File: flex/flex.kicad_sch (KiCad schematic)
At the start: 93 parts, among them J1 Conn_01x06_Female, J2 Conn_01x05_Female, J3 Conn_01x03_Female, J4 Conn_01x06_Female, J5 Conn_01x03_Female, SW1 SW_Push, SW10 SW_Push, SW11 SW_Push, SW12 SW_Push, SW14 SW_Push, SW15 SW_Push, SW16 SW_Push, SW17 SW_Push, SW19 SW_Push, SW2 SW_Push, SW20 SW_Push, SW21 SW_Push, SW22 SW_Push, SW23 SW_Push, SW24 SW_Push, SW25 SW_Push, SW26 SW_Push, SW3 SW_Push, SW4 SW_Push, SW5 SW_Push, SW6 SW_Push, SW7 SW_Push, SW8 SW_Push, SW9 SW_Push

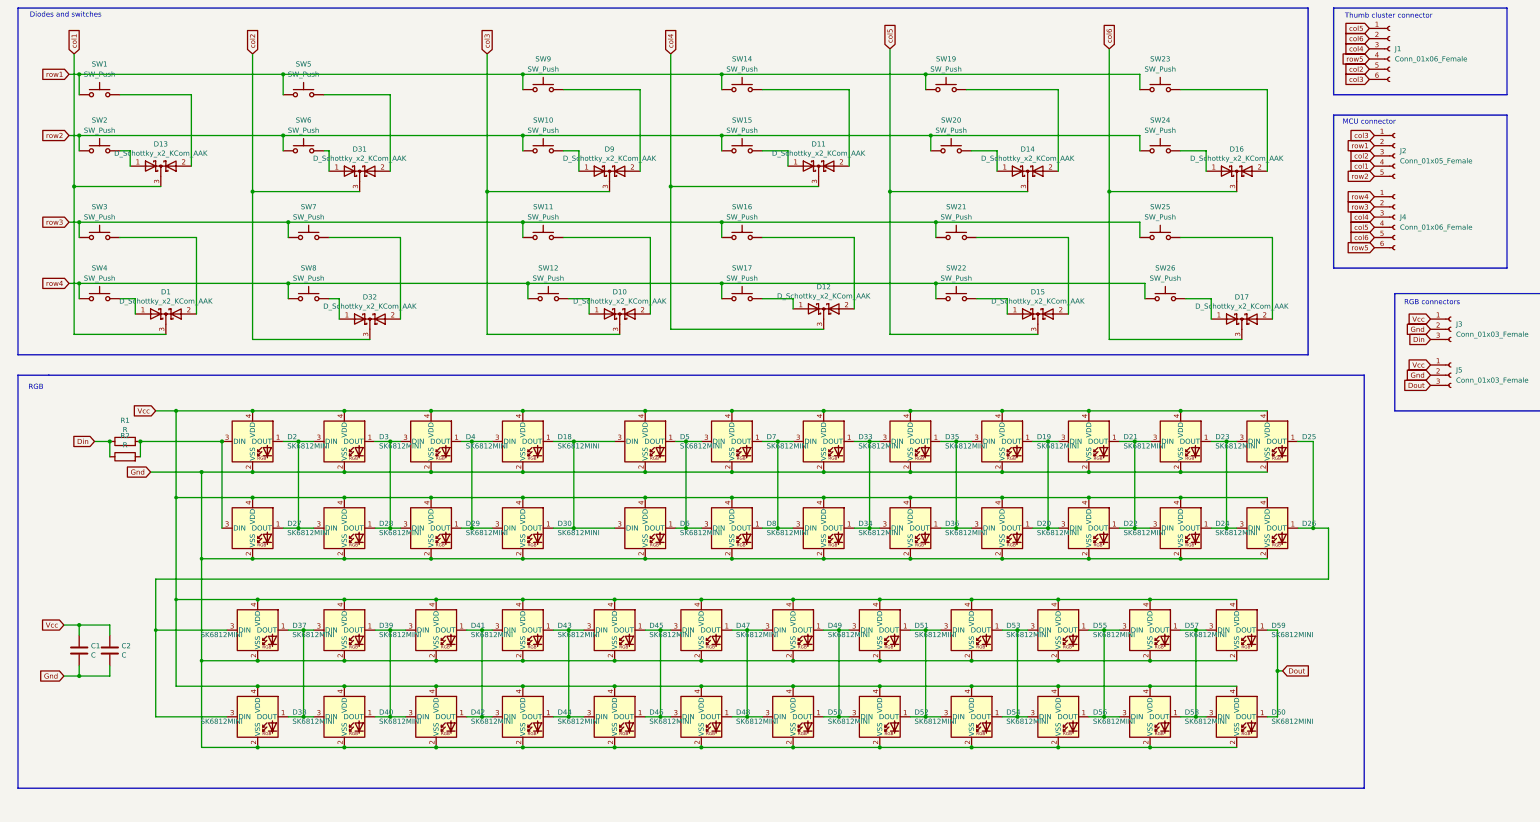
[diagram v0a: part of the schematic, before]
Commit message: update diodes and leds
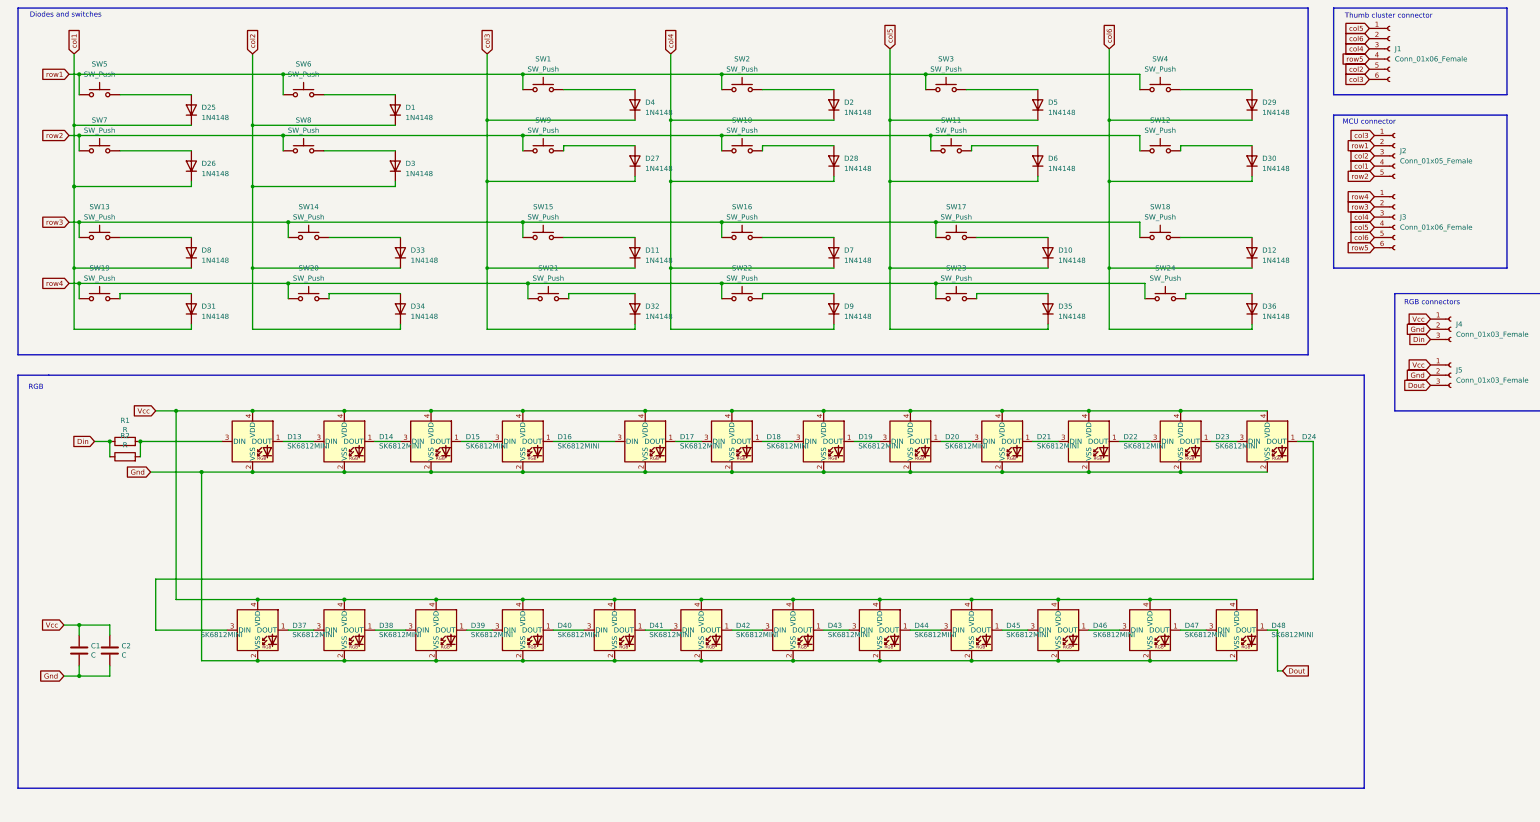
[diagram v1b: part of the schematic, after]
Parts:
- removed D1, D10, D11, D12, D13, D14, D15, D16, D17, D31, D32, D9: D_Schottky_x2_KCom_AAK, customs:TSOT-23_HandSoldering, symbol Device:D_Schottky_x2_KCom_AAK
- removed D20, D22, D24, D26, D27, D28, D29, D30, D34, D36, D38, D40, D42, D44, D46, D48, D50, D52, D54, D56, D58, D6, D60, D8: SK6812MINI, libs2:YS-SK6812MINI-E_REVERSE_NO_EDGECUT, symbol LED:SK6812MINI
- added D1, D10, D11, D12, D2, D25, D26, D27, D28, D29, D3, D30, D31, D32, D33, D34, D35, D36, D4, D5, D6, D7, D8, D9: 1N4148, libs:D_0402, symbol Diode:1N4148
- D13: renamed from D2; footprint libs2:YS-SK6812MINI-E_REVERSE -> libs:SK6812_mini_e_corners
- D14: renamed from D3; footprint libs2:YS-SK6812MINI-E_REVERSE -> libs:SK6812_mini_e_corners
- D15: renamed from D4; footprint libs2:YS-SK6812MINI-E_REVERSE -> libs:SK6812_mini_e_corners
- D16: renamed from D18; footprint libs2:YS-SK6812MINI-E_REVERSE -> libs:SK6812_mini_e_corners
- D17: renamed from D5; footprint libs2:YS-SK6812MINI-E_REVERSE -> libs:SK6812_mini_e_corners
- D18: renamed from D7; footprint libs2:YS-SK6812MINI-E_REVERSE -> libs:SK6812_mini_e_corners
- D19: renamed from D33; footprint libs2:YS-SK6812MINI-E_REVERSE -> libs:SK6812_mini_e_corners
- D20: renamed from D35; footprint libs2:YS-SK6812MINI-E_REVERSE -> libs:SK6812_mini_e_corners
- D21: renamed from D19; footprint libs2:YS-SK6812MINI-E_REVERSE -> libs:SK6812_mini_e_corners
- D22: renamed from D21; footprint libs2:YS-SK6812MINI-E_REVERSE -> libs:SK6812_mini_e_corners
- D23, D37: footprint libs2:YS-SK6812MINI-E_REVERSE -> libs:SK6812_mini_e_corners
- D24: renamed from D25; footprint libs2:YS-SK6812MINI-E_REVERSE -> libs:SK6812_mini_e_corners
- D38: renamed from D39; footprint libs2:YS-SK6812MINI-E_REVERSE -> libs:SK6812_mini_e_corners
- D39: renamed from D41; footprint libs2:YS-SK6812MINI-E_REVERSE -> libs:SK6812_mini_e_corners
- D40: renamed from D43; footprint libs2:YS-SK6812MINI-E_REVERSE -> libs:SK6812_mini_e_corners
- D41: renamed from D45; footprint libs2:YS-SK6812MINI-E_REVERSE -> libs:SK6812_mini_e_corners
- D42: renamed from D47; footprint libs2:YS-SK6812MINI-E_REVERSE -> libs:SK6812_mini_e_corners
- D43: renamed from D49; footprint libs2:YS-SK6812MINI-E_REVERSE -> libs:SK6812_mini_e_corners
- D44: renamed from D51; footprint libs2:YS-SK6812MINI-E_REVERSE -> libs:SK6812_mini_e_corners
- D45: renamed from D53; footprint libs2:YS-SK6812MINI-E_REVERSE -> libs:SK6812_mini_e_corners
- D46: renamed from D55; footprint libs2:YS-SK6812MINI-E_REVERSE -> libs:SK6812_mini_e_corners
- D47: renamed from D57; footprint libs2:YS-SK6812MINI-E_REVERSE -> libs:SK6812_mini_e_corners
- D48: renamed from D59; footprint libs2:YS-SK6812MINI-E_REVERSE -> libs:SK6812_mini_e_corners
- renumbered J4 to J3, J3 to J4, SW9 to SW1, SW15 to SW10, SW20 to SW11, SW24 to SW12, SW3 to SW13, SW7 to SW14, SW11 to SW15, SW21 to SW17, SW25 to SW18, SW4 to SW19, SW14 to SW2, SW8 to SW20, SW12 to SW21, SW17 to SW22, SW22 to SW23, SW26 to SW24, SW19 to SW3, SW23 to SW4, SW1 to SW5, SW5 to SW6, SW2 to SW7, SW6 to SW8, SW10 to SW9
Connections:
- net col1: now also D25.1 (K), D26.1 (K), D31.1 (K), D8.1 (K)
- net col2: now also D1.1 (K), D3.1 (K), D33.1 (K), D34.1 (K)
- net col3: now also D11.1 (K), D27.1 (K), D32.1 (K), D4.1 (K)
- net col4: now also D2.1 (K), D28.1 (K), D7.1 (K), D9.1 (K)
- net col5: now also D10.1 (K), D35.1 (K), D5.1 (K), D6.1 (K)
- net col6: now also D12.1 (K), D29.1 (K), D30.1 (K), D36.1 (K)
- net at SW23.2: now also D35.2 (A)
- net at SW17.2: now also D10.2 (A)
- net at SW7.2: now also D26.2 (A)
- net at SW24.2: now also D36.2 (A)
- net at SW18.2: now also D12.2 (A)
- net at SW6.2: now also D1.2 (A)
- net at SW15.2: now also D11.2 (A)
- net at SW21.2: now also D32.2 (A)
- net at SW20.2: now also D34.2 (A)
- net at SW22.2: now also D9.2 (A)
- net at SW16.2: now also D7.2 (A)
- net at SW8.2: now also D3.2 (A)
- net at SW5.2: now also D25.2 (A)
- net at SW13.2: now also D8.2 (A)
- net at SW2.2: now also D2.2 (A)
- net at SW12.2: now also D30.2 (A)
- net at SW9.2: now also D27.2 (A)
- net at SW1.2: now also D4.2 (A)
- net at SW11.2: now also D6.2 (A)
- net at SW10.2: now also D28.2 (A)
- net at SW19.2: now also D31.2 (A)
- net at SW3.2: now also D5.2 (A)
- net at SW14.2: now also D33.2 (A)
- net at SW4.2: now also D29.2 (A)

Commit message: emergency diodes
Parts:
- added D49, D50, D51, D52, D53, D54, D55, D56, D57, D58, D59, D60, D61, D62, D63, D64, D65, D66, D67, D68, D69, D70, D71, D72: 1N4148, custom:Diode_TH_SOD123, symbol Diode:1N4148
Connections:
- net col1: now also D49.1 (K), D50.1 (K), D51.1 (K), D52.1 (K)
- net col2: now also D53.1 (K), D54.1 (K), D55.1 (K), D56.1 (K)
- net col3: now also D57.1 (K), D58.1 (K), D59.1 (K), D60.1 (K)
- net col4: now also D61.1 (K), D62.1 (K), D63.1 (K), D64.1 (K)
- net col5: now also D65.1 (K), D66.1 (K), D67.1 (K), D68.1 (K)
- net col6: now also D69.1 (K), D70.1 (K), D71.1 (K)
- net at D26.2 (A), SW7.2: now also D50.2 (A)
- net at D25.2 (A), SW5.2: now also D49.2 (A)
- net at D35.2 (A), SW23.2: now also D68.2 (A)
- net at D28.2 (A), SW10.2: now also D62.2 (A)
- net at D7.2 (A), SW16.2: now also D63.2 (A)
- net at D30.2 (A), SW12.2: now also D70.2 (A)
- net at D11.2 (A), SW15.2: now also D59.2 (A)
- net at D27.2 (A), SW9.2: now also D58.2 (A)
- net at D1.2 (A), SW6.2: now also D53.2 (A)
- net at D32.2 (A), SW21.2: now also D60.2 (A)
- net at D34.2 (A), SW20.2: now also D56.2 (A)
- net at D3.2 (A), SW8.2: now also D54.2 (A)
- net at D8.2 (A), SW13.2: now also D51.2 (A)
- net at D6.2 (A), SW11.2: now also D66.2 (A)
- net at D2.2 (A), SW2.2: now also D61.2 (A)
- net at D31.2 (A), SW19.2: now also D52.2 (A)
- net at D9.2 (A), SW22.2: now also D64.2 (A)
- net at D12.2 (A), SW18.2: now also D71.2 (A)
- net at D10.2 (A), SW17.2: now also D67.2 (A)
- net at D4.2 (A), SW1.2: now also D57.2 (A)
- net at D33.2 (A), SW14.2: now also D55.2 (A)
- net at D5.2 (A), SW3.2: now also D65.2 (A)
- net at D29.2 (A), SW4.2: now also D69.2 (A)
- net at D36.2 (A), SW24.2: now also D72.2 (A)

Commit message: routing
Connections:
- net col6: now also D72.1 (K)
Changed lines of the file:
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@@
   (junction (at 125.73 119.38) (diameter 1.016) (color 0 0 0 0)
   )
+  (junction (at 317.5 99.06) (diameter 0) (color 0 0 0 0)
+  )
   (junction (at 213.36 76.2) (diameter 0) (color 0 0 0 0)
   )
@@
     (stroke (width 0) (type default))
   )
-  (wire (pts (xy 294.64 99.06) (xy 330.2 99.06))
+  (wire (pts (xy 294.64 99.06) (xy 317.5 99.06))
     (stroke (width 0) (type solid))
   )
@@
     (stroke (width 0) (type solid))
   )
+  (wire (pts (xy 317.5 97.79) (xy 317.5 99.06))
+    (stroke (width 0) (type default))
+  )
   (wire (pts (xy 99.06 40.64) (xy 106.68 40.64))
     (stroke (width 0) (type solid))
@@
     (stroke (width 0) (type solid))
   )
+  (wire (pts (xy 317.5 99.06) (xy 330.2 99.06))
+    (stroke (width 0) (type solid))
+  )

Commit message: routing
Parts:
- removed C2: C, Capacitor_SMD:C_1206_3216Metric_Pad1.42x1.75mm_HandSolder, symbol Device:C
- removed R2: R, Resistor_SMD:R_1206_3216Metric_Pad1.42x1.75mm_HandSolder, symbol Device:R
- added C3: C, custom:C_SOD123, symbol Device:C
- added R3: R, custom:R_SOD123, symbol Device:R
- C1: footprint Capacitor_SMD:C_1206_3216Metric_Pad1.42x1.75mm_HandSolder -> libs:D_0402
- R1: footprint Resistor_SMD:R_1206_3216Metric_Pad1.42x1.75mm_HandSolder -> libs:D_0402
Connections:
- net Din: now also R3.1
- net Gnd: now also C3.2
- net Vcc: now also C3.1
- net at D13.3 (DIN), R1.2: now also R3.2
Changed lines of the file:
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@@
     (stroke (width 0) (type solid))
   )
-  (wire (pts (xy 45.72 127) (xy 45.72 130.81))
-    (stroke (width 0) (type solid))
-  )
   (wire (pts (xy 185.42 46.99) (xy 185.42 62.23))
     (stroke (width 0) (type solid))
@@
     (stroke (width 0) (type default))
   )
+  (wire (pts (xy 45.72 175.26) (xy 52.07 175.26))
+    (stroke (width 0) (type default))
+  )
   (wire (pts (xy 214.63 53.34) (xy 226.06 53.34))
     (stroke (width 0) (type solid))
@@
     (stroke (width 0) (type solid))
   )
+  (wire (pts (xy 45.72 182.88) (xy 52.07 182.88))
+    (stroke (width 0) (type default))
+  )
   (wire (pts (xy 35.56 50.8) (xy 38.1 50.8))
     (stroke (width 0) (type solid))
@@
     (stroke (width 0) (type default))
   )
+  (wire (pts (xy 45.72 127) (xy 45.72 134.62))
+    (stroke (width 0) (type default))
+  )
   (wire (pts (xy 275.59 127) (xy 281.94 127))
     (stroke (width 0) (type solid))
@@
     (stroke (width 0) (type solid))
   )
+  (wire (pts (xy 55.88 134.62) (xy 55.88 144.78))
+    (stroke (width 0) (type solid))
+  )
   (wire (pts (xy 36.83 83.82) (xy 54.61 83.82))
     (stroke (width 0) (type default))
@@
     (stroke (width 0) (type solid))
   )
-  (wire (pts (xy 53.34 127) (xy 53.34 130.81))
+  (wire (pts (xy 53.34 127) (xy 53.34 134.62))
     (stroke (width 0) (type solid))
   )
@@
     )
   )
-  (global_label "Gnd" (shape input) (at 55.88 134.62 180)
+  (global_label "Gnd" (shape input) (at 55.88 144.78 180)
     (effects (font (size 1.27 1.27)) (justify right))
-    (property "Intersheetrefs" "${INTERSHEET_REFS}" (at 25.4 -3.81 0)
+    (property "Intersheetrefs" "${INTERSHEET_REFS}" (at 25.4 6.35 0)
       (effects (font (size 1.27 1.27)) hide)
     )
@@
       (effects (font (size 1.27 1.27)) (justify left))
     )
-    (property "Footprint" "Capacitor_SMD:C_1206_3216Metric_Pad1.42x1.75mm_HandSolder" (at 39.0652 182.88 0)
+    (property "Footprint" "libs:D_0402" (at 39.0652 182.88 0)
       (effects (font (size 1.27 1.27)) hide)
     )
@@
     )
   )
-  (symbol (lib_id "Device:C") (at 45.72 179.07 0) (unit 1)
-    (in_bom yes) (on_board yes) (dnp no)
-    (property "Reference" "C2" (at 48.6411 177.9206 0)
-      (effects (font (size 1.27 1.27)) (justify left))
-    )
-    (property "Value" "C" (at 48.6411 180.2193 0)
-      (effects (font (size 1.27 1.27)) (justify left))
-    )
-    (property "Footprint" "Capacitor_SMD:C_1206_3216Metric_Pad1.42x1.75mm_HandSolder" (at 46.6852 182.88 0)
-      (effects (font (size 1.27 1.27)) hide)
-    )
-    (property "Datasheet" "~" (at 45.72 179.07 0)
-      (effects (font (size 1.27 1.27)) hide)
-    )
-    (pin "1")
-    (pin "2")
-    (instances
-      (project "flex"
-        (path "/e63e39d7-6ac0-4ffd-8aa3-1841a4541b55"
-          (reference "C2") (unit 1)
-        )
-      )
-    )
-  )
   (symbol (lib_id "Switch:SW_Push") (at 203.2 39.37 0) (unit 1)
     (in_bom yes) (on_board yes) (dnp no)
@@
     )
   )
-  (symbol (lib_id "Device:R") (at 49.53 130.81 90) (unit 1)
-    (in_bom yes) (on_board yes) (dnp no)
-    (property "Reference" "R2" (at 49.53 125.5838 90)
-      (effects (font (size 1.27 1.27)))
-    )
-    (property "Value" "R" (at 49.53 127.8825 90)
-      (effects (font (size 1.27 1.27)))
-    )
-    (property "Footprint" "Resistor_SMD:R_1206_3216Metric_Pad1.42x1.75mm_HandSolder" (at 49.53 132.588 90)
-      (effects (font (size 1.27 1.27)) hide)
-    )
-    (property "Datasheet" "~" (at 49.53 130.81 0)
-      (effects (font (size 1.27 1.27)) hide)
-    )
-    (pin "1")
-    (pin "2")
-    (instances
-      (project "flex"
-        (path "/e63e39d7-6ac0-4ffd-8aa3-1841a4541b55"
-          (reference "R2") (unit 1)
-        )
-      )
-    )
-  )
   (symbol (lib_id "Diode:1N4148") (at 214.63 57.15 90) (unit 1)
     (in_bom yes) (on_board yes) (dnp no) (fields_autoplaced)
@@
       (effects (font (size 1.27 1.27)))
     )
-    (property "Footprint" "Resistor_SMD:R_1206_3216Metric_Pad1.42x1.75mm_HandSolder" (at 49.53 128.778 90)
+    (property "Footprint" "libs:D_0402" (at 49.53 128.778 90)
       (effects (font (size 1.27 1.27)) hide)
     )
@@
     )
   )
+  (symbol (lib_id "Device:R") (at 49.53 134.62 90) (unit 1)
+    (in_bom yes) (on_board yes) (dnp no)
+    (property "Reference" "R3" (at 49.53 129.3938 90)
+      (effects (font (size 1.27 1.27)))
+    )
+    (property "Value" "R" (at 49.53 131.6925 90)
+      (effects (font (size 1.27 1.27)))
+    )
+    (property "Footprint" "custom:R_SOD123" (at 49.53 136.398 90)
+      (effects (font (size 1.27 1.27)) hide)
+    )
+    (property "Datasheet" "~" (at 49.53 134.62 0)
+      (effects (font (size 1.27 1.27)) hide)
+    )
+    (pin "1")
+    (pin "2")
+    (instances
+      (project "flex"
+        (path "/e63e39d7-6ac0-4ffd-8aa3-1841a4541b55"
+          (reference "R3") (unit 1)
+        )
+      )
+    )
+  )
   (symbol (lib_id "Diode:1N4148") (at 66.04 80.01 90) (unit 1)
     (in_bom yes) (on_board yes) (dnp no) (fields_autoplaced)
@@
         )
       )
+    )
+  )
+  (symbol (lib_id "Device:C") (at 52.07 179.07 0) (unit 1)
+    (in_bom yes) (on_board yes) (dnp no)
+    (property "Reference" "C3" (at 54.9911 177.9206 0)
+      (effects (font (size 1.27 1.27)) (justify left) hide)
+    )
+    (property "Value" "C" (at 54.9911 180.2193 0)
+      (effects (font (size 1.27 1.27)) (justify left))
+    )
+    (property "Footprint" "custom:C_SOD123" (at 53.0352 182.88 0)
+      (effects (font (size 1.27 1.27)) hide)
+    )
+    (property "Datasheet" "~" (at 52.07 179.07 0)
+      (effects (font (size 1.27 1.27)) hide)
+    )
+    (pin "1")
+    (pin "2")
+    (instances
+      (project "flex"
+        (path "/e63e39d7-6ac0-4ffd-8aa3-1841a4541b55"
+          (reference "C3") (unit 1)
+        )
+      )

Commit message: bom
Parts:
- C3: value C -> C3; now left out of the parts list
- D13, D14, D15, D16, D17, D18, D19, D20, D21, D22, D23, D24, D37, D38, D39, D40, D41, D42, D43, D44, D45, D46, D47, D48, D49, D50, D51, D52, D53, D54, D55, D56, D57, D58, D59, D60, D61, D62, D63, D64, D65, D66, D67, D68, D69, D70, D71, D72, J1, J2, J3, J4, J5, R3, SW1, SW10, SW11, SW12, SW13, SW14, SW15, SW16, SW17, SW18, SW19, SW2, SW20, SW21, SW22, SW23, SW24, SW3, SW4, SW5, SW6, SW7, SW8, SW9: now left out of the parts list
